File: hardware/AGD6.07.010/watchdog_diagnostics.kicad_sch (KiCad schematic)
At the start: 11 parts, among them U1 TPS3430WDRC, U3 TMP117AIDRVR

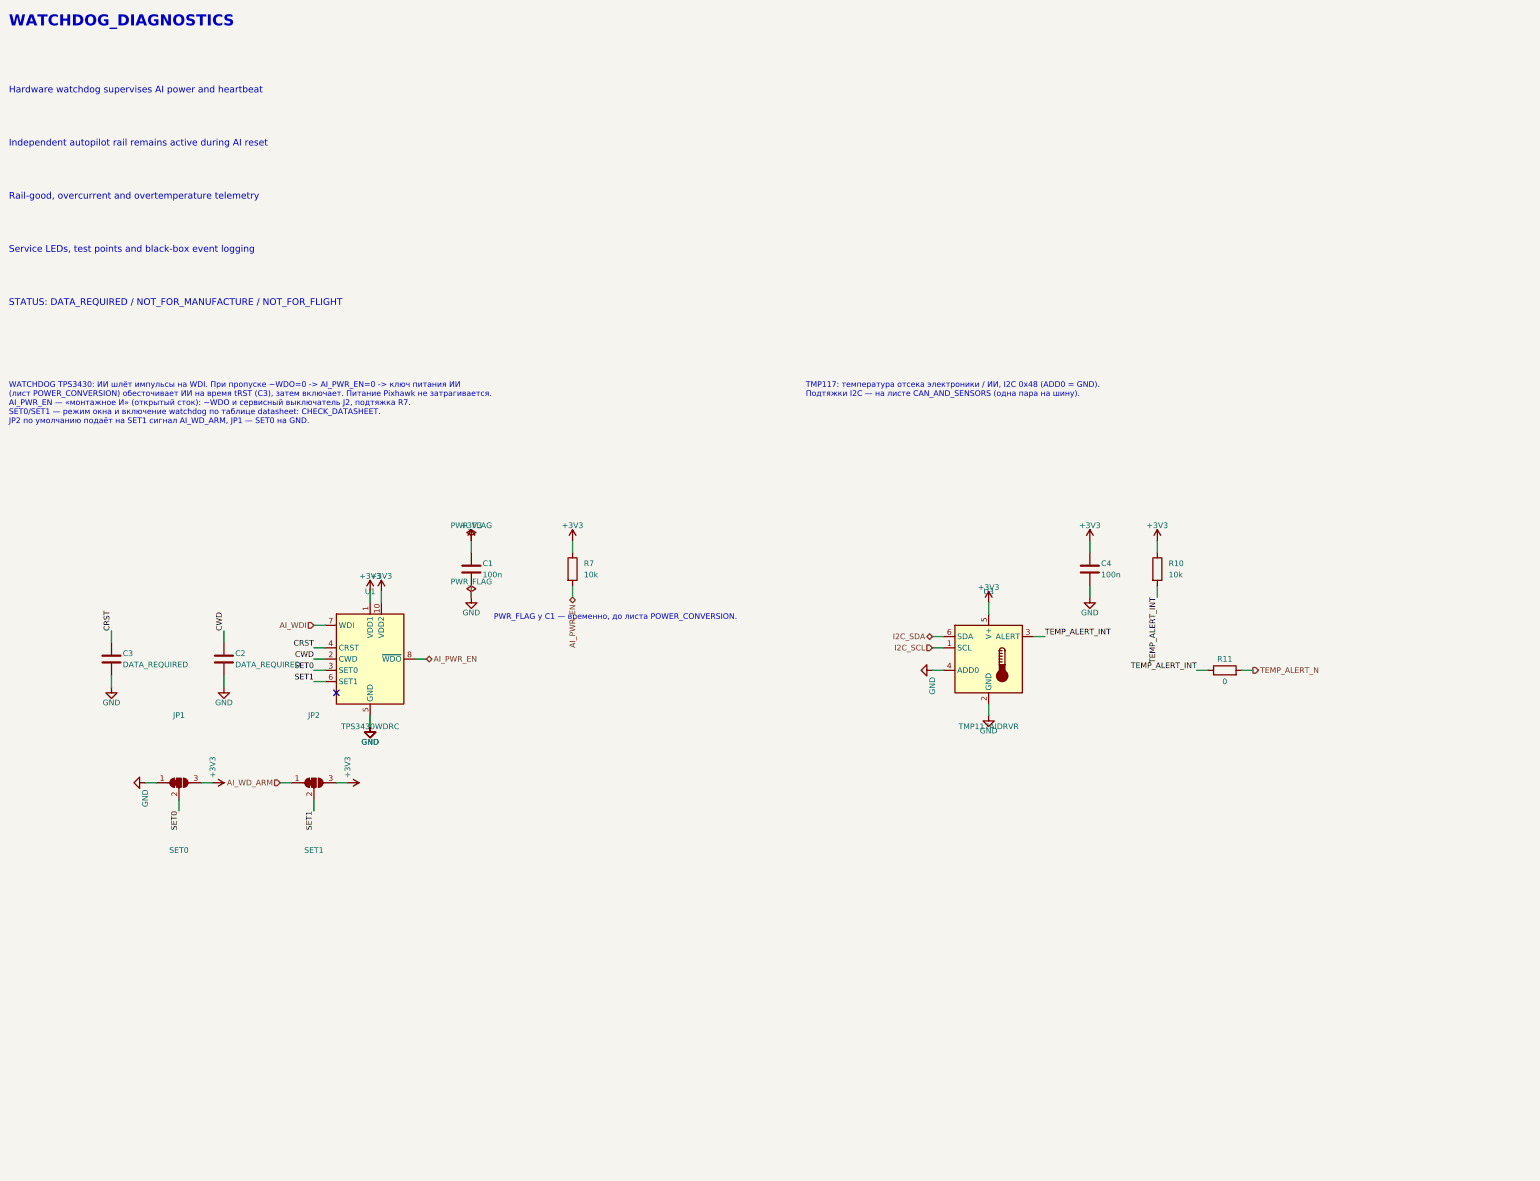
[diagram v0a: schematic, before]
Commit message: Draw full AGD6.07.010 schematic per integrated_avionics_board spec
All ten sheets now carry components: 14S input with hot-swap and power
monitor, 12/5/3.3 V rails and a separate 12 V AI channel with soft-start
and current telemetry, Pixhawk connectors, CAN1/CAN2 hub with chokes,
ESD and switchable termination, sensor conditioning, SIYI and radar,
AI interface and watchdog, protected 12 V switches with diagnostics,
fan/heater control, cameras and Ethernet. Open choices are recorded in
DECISIONS.md; datasheet-dependent values are flagged CHECK_DATASHEET.

ERC: no errors. All 752 intended pin connections match the KiCad netlist.

Co-Authored-By: Claude Opus 5.5 <noreply@anthropic.com>
Claude-Session: https://claude.ai/code/session_01Qk7uTKdi6YbndB9fGuguYV
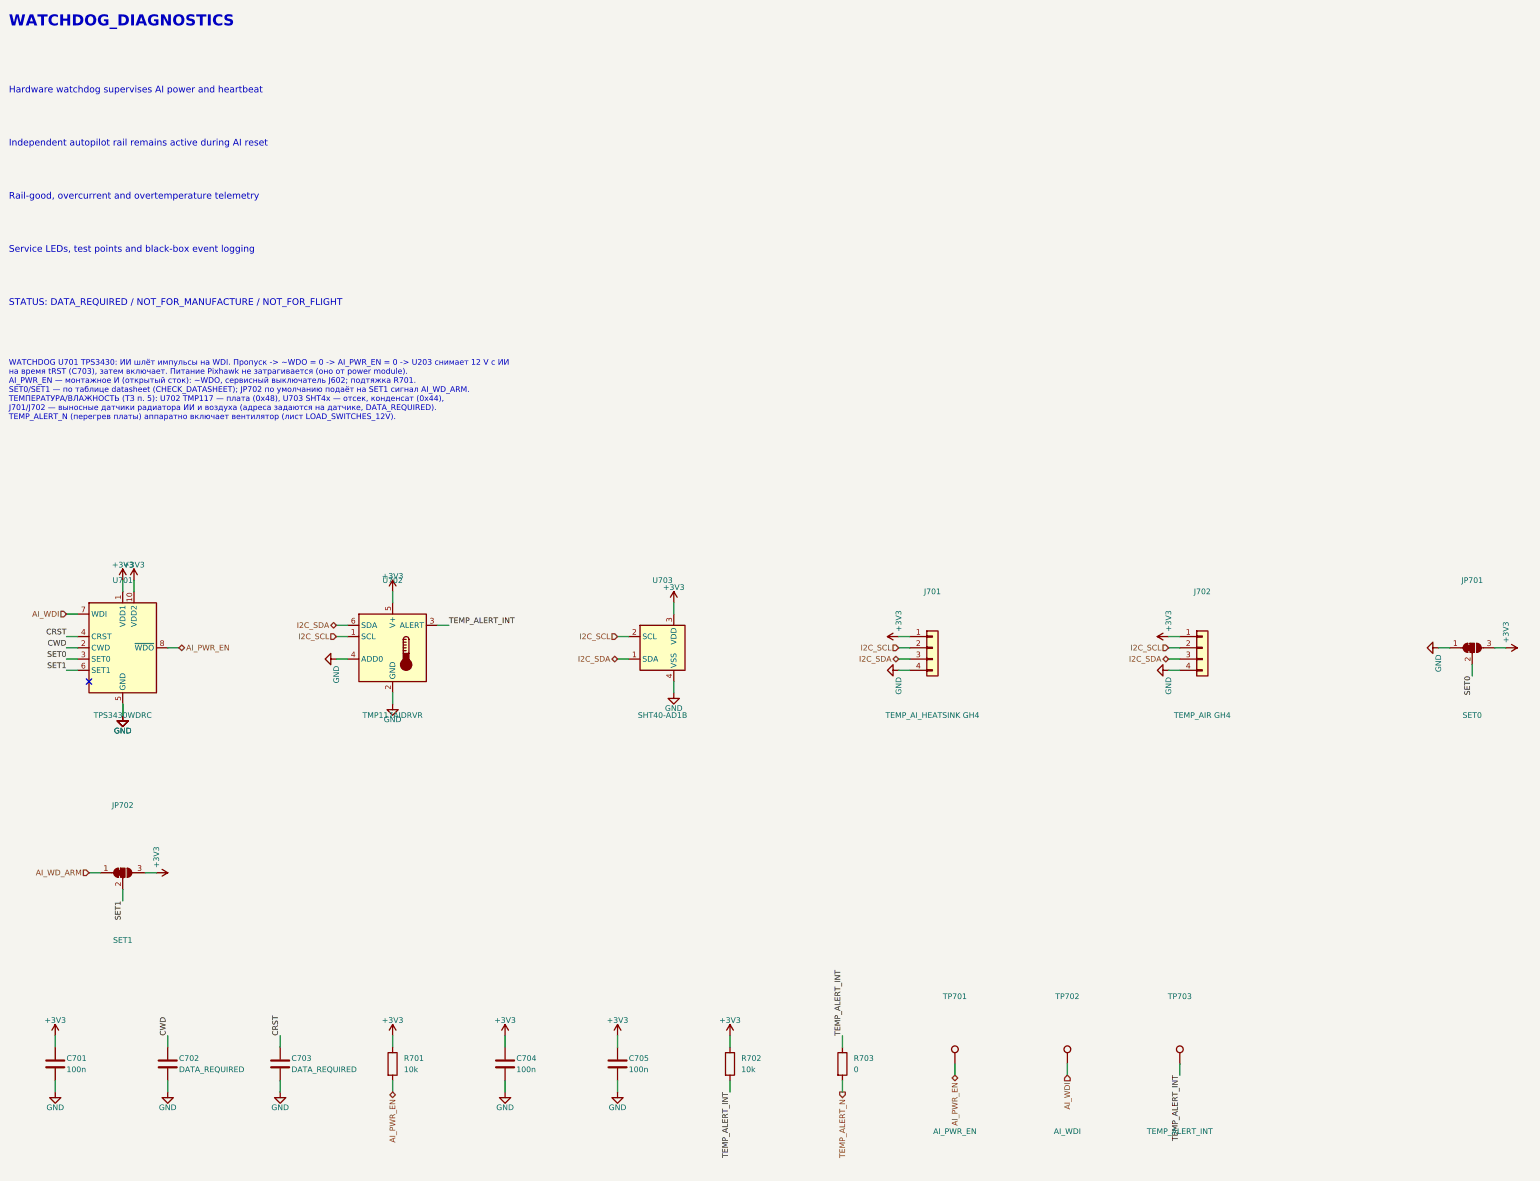
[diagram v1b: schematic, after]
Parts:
- removed C1, C4: 100n, Capacitor_SMD:C_0402_1005Metric, symbol Device:C
- removed C2, C3: DATA_REQUIRED, Capacitor_SMD:C_0402_1005Metric, symbol Device:C
- removed JP1: SET0, Jumper:SolderJumper-3_P1.3mm_Bridged12_RoundedPad1.0x1.5mm_NumberLabels, symbol Jumper:SolderJumper_3_Bridged12
- removed JP2: SET1, Jumper:SolderJumper-3_P1.3mm_Bridged12_RoundedPad1.0x1.5mm_NumberLabels, symbol Jumper:SolderJumper_3_Bridged12
- removed R10, R7: 10k, Resistor_SMD:R_0402_1005Metric, symbol Device:R
- removed R11: 0, Resistor_SMD:R_0402_1005Metric, symbol Device:R
- removed U1: TPS3430WDRC, Package_SON:VSON-10-1EP_3x3mm_P0.5mm_EP1.65x2.4mm, symbol Power_Supervisor:TPS3430WDRC
- removed U3: TMP117AIDRVR, Package_SON:WSON-6-1EP_2x2mm_P0.65mm_EP1x1.6mm, symbol Sensor_Temperature:TMP117xxDRV
- added C701, C704, C705: 100n, Capacitor_SMD:C_0402_1005Metric, symbol Device:C
- added C702, C703: DATA_REQUIRED, Capacitor_SMD:C_0402_1005Metric, symbol Device:C
- added J701: TEMP_AI_HEATSINK GH4, Connector_JST:JST_GH_SM04B-GHS-TB_1x04-1MP_P1.25mm_Horizontal, symbol Connector_Generic:Conn_01x04
- added J702: TEMP_AIR GH4, Connector_JST:JST_GH_SM04B-GHS-TB_1x04-1MP_P1.25mm_Horizontal, symbol Connector_Generic:Conn_01x04
- added JP701: SET0, Jumper:SolderJumper-3_P1.3mm_Bridged12_RoundedPad1.0x1.5mm_NumberLabels, symbol Jumper:SolderJumper_3_Bridged12
- added JP702: SET1, Jumper:SolderJumper-3_P1.3mm_Bridged12_RoundedPad1.0x1.5mm_NumberLabels, symbol Jumper:SolderJumper_3_Bridged12
- added R701, R702: 10k, Resistor_SMD:R_0402_1005Metric, symbol Device:R
- added R703: 0, Resistor_SMD:R_0402_1005Metric, symbol Device:R
- added TP701: AI_PWR_EN, TestPoint:TestPoint_Pad_D1.5mm, symbol Connector:TestPoint
- added TP702: AI_WDI, TestPoint:TestPoint_Pad_D1.5mm, symbol Connector:TestPoint
- added TP703: TEMP_ALERT_INT, TestPoint:TestPoint_Pad_D1.5mm, symbol Connector:TestPoint
- added U701: TPS3430WDRC, Package_SON:VSON-10-1EP_3x3mm_P0.5mm_EP1.65x2.4mm, symbol Power_Supervisor:TPS3430WDRC
- added U702: TMP117AIDRVR, Package_SON:WSON-6-1EP_2x2mm_P0.65mm_EP1x1.6mm, symbol Sensor_Temperature:TMP117xxDRV
- added U703: SHT40-AD1B, Sensor_Humidity:Sensirion_DFN-4_1.5x1.5mm_P0.8mm_SHT4x_NoCentralPad, symbol Sensor_Humidity:SHT4x
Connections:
- net +3V3: now also C701.1, C704.1, C705.1, J701.1 (Pin_1), J702.1 (Pin_1), JP701.3 (B), JP702.3 (B), R701.1, R702.1, U701.1 (VDD1), U701.10 (VDD2), U702.5 (V+), U703.3 (VDD)
- net AI_PWR_EN: now also R701.2, TP701.1, U701.8 (~{WDO})
- net AI_WDI: now also TP702.1, U701.7 (WDI)
- net AI_WD_ARM: now also JP702.1 (A)
- net CRST: now also C703.1, U701.4 (CRST)
- net CWD: now also C702.1, U701.2 (CWD)
- net GND: now also C701.2, C702.2, C703.2, C704.2, C705.2, J701.4 (Pin_4), J702.4 (Pin_4), JP701.1 (A), U701.11 (GND), U701.5 (GND), U702.2 (GND), U702.4 (ADD0), U703.4 (VSS)
- net I2C_SCL: now also J701.2 (Pin_2), J702.2 (Pin_2), U702.1 (SCL), U703.2 (SCL)
- net I2C_SDA: now also J701.3 (Pin_3), J702.3 (Pin_3), U702.6 (SDA), U703.1 (SDA)
- net SET0: now also JP701.2 (C), U701.3 (SET0)
- net SET1: now also JP702.2 (C), U701.6 (SET1)
- net TEMP_ALERT_INT: now also R702.2, R703.1, TP703.1, U702.3 (ALERT)
- net TEMP_ALERT_N: now also R703.2
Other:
- note added: "WATCHDOG U701 TPS3430: ИИ шлёт импульсы на WDI. Пропуск -> ~WDO = 0 -> AI_PWR_EN = 0 -> U203 снимает 12 V с ИИ на время tRST (C703), затем включает. Питание Pixhawk не затрагивается (оно от power module). AI_PWR_EN — монтажное И (открытый сток): ~WDO, сервисный выключатель J602; подтяжка R701. SET0/SET1 — по таблице datasheet (CHECK_DATASHEET); JP702 по умолчанию подаёт на SET1 сигнал AI_WD_ARM. 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"
- note removed: "PWR_FLAG у C1 — временно, до листа POWER_CONVERSION."
- note removed: "TMP117: температура отсека электроники / ИИ, I2C 0x48 (ADD0 = GND). Подтяжки I2C — на листе CAN_AND_SENSORS (одна пара на шину)."
- note removed: "WATCHDOG TPS3430: ИИ шлёт импульсы на WDI. При пропуске ~WDO=0 -> AI_PWR_EN=0 -> ключ питания ИИ (лист POWER_CONVERSION) обесточивает ИИ на время tRST (C3), затем включает. Питание Pixhawk не затрагивается. AI_PWR_EN — «монтажное И» (открытый сток): ~WDO и сервисный выключатель J2, подтяжка R7. SET0/SET1 — режим окна и включение watchdog по таблице datasheet: CHECK_DATASHEET. JP2 по умолчанию под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"

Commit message: AGD6.07.010 rev 0.3: design review fixes and bring-up plan
Design review (DESIGN_REVIEW.md) with fixes applied to the schematic:
INA228 input RC filters, 12 V bus current monitor (INA228 0x45),
BTS5030 diagnostic scaling with clamp diodes, flow input level fix,
CAN1 changed from star to daisy chain with on-board terminator, AI
shutdown request, board buzzer, series resistors and ESD on external
I2C probes. Connectors merged so every connector sits on a board edge.
Adds calculations.md (power, IPC-2221 widths, hot-swap, thermal, ADC
scaling, CAN, clearances) and BRINGUP.md (step-by-step test plan).
ERC: no errors; all 820 intended pin connections verified. Board is
re-placed; routing in progress.

Co-Authored-By: Claude Opus 5.5 <noreply@anthropic.com>
Claude-Session: https://claude.ai/code/session_01Qk7uTKdi6YbndB9fGuguYV
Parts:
- added R704, R705: 33, Resistor_SMD:R_0402_1005Metric, symbol Device:R
- added U704: TPD4E05U06DQA, Package_SON:USON-10_2.5x1.0mm_P0.5mm, symbol Power_Protection:TPD4E05U06DQA
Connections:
- net GND: now also U704.3 (GND), U704.8 (GND)
- net I2C_SCL: now also R704.1; no longer J701.2 (Pin_2), J702.2 (Pin_2)
- net I2C_SDA: now also R705.1; no longer J701.3 (Pin_3), J702.3 (Pin_3)
- new net P_SCL: J701.2 (Pin_2), J702.2 (Pin_2), R704.2, U704.1 (D1+)
- new net P_SDA: J701.3 (Pin_3), J702.3 (Pin_3), R705.2, U704.2 (D1-)
- no-connect marks 1 -> 7

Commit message: AGD6.07.010 rev 0.4 (WIP): 3x TRACO THL40 DC/DC, split 12 V bus, SwitchBlox Ethernet, fixed LM5069 UVLO/OVLO, computed hot-swap values, PX4 firmware notes; board re-placed, routing in progress
Co-Authored-By: Claude Opus 5.5 <noreply@anthropic.com>
Claude-Session: https://claude.ai/code/session_01Qk7uTKdi6YbndB9fGuguYV
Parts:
- C702: value DATA_REQUIRED -> DNP; Note CHECK_DATASHEET -> РАСЧЁТ: calculations.md; Purpose таймаут watchdog -> не ставить: CWD свободен = заводской таймаут (TI TPS3430); now not fitted
- C703: value DATA_REQUIRED -> DNP; Note CHECK_DATASHEET -> РАСЧЁТ: calculations.md; Purpose время отключения ИИ ~1 с -> не ставить: CRST свободен = заводская задержка сброса; now not fitted
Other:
- note added: "WATCHDOG U701 TPS3430: ИИ шлёт импульсы на WDI. Пропуск -> ~WDO = 0 -> AI_PWR_EN = 0 -> U203 снимает 12 V с ИИ на время заводской задержки tRST (C703 не ставится), затем включает. Питание Pixhawk не затрагивается (оно от power module). AI_PWR_EN — монтажное И (открытый сток): ~WDO, сервисный выключатель J602; подтяжка R701. SET0/SET1 — по таблице datasheet (CHECK_DATASHEET); JP702 по умолчанию по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"
- note removed: "WATCHDOG U701 TPS3430: ИИ шлёт импульсы на WDI. Пропуск -> ~WDO = 0 -> AI_PWR_EN = 0 -> U203 снимает 12 V с ИИ на время tRST (C703), затем включает. Питание Pixhawk не затрагивается (оно от power module). AI_PWR_EN — монтажное И (открытый сток): ~WDO, сервисный выключатель J602; подтяжка R701. SET0/SET1 — по таблице datasheet (CHECK_DATASHEET); JP702 по умолчанию подаёт на SET1 сигнал AI_WD_ARM. 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"
